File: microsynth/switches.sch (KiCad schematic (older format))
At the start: 39 parts, among them SW12 SW_DP3T, SW13 SW_DP3T, SW14 SW_SPDT, SW15 SW_SPDT, SW16 SW_SPDT, SW17 SW_SPDT, SW2 SW_Rotary2x6, SW21 SW_Rotary2x6, SW3 SW_DP3T, SW4 SW_DP3T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

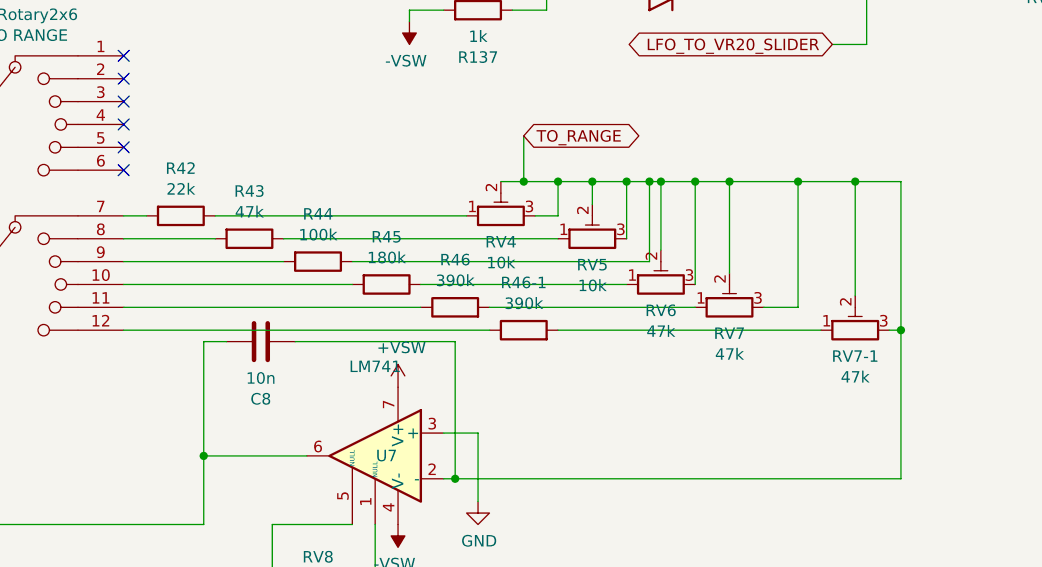
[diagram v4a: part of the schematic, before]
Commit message: Replace IC1 with LM348, update component values
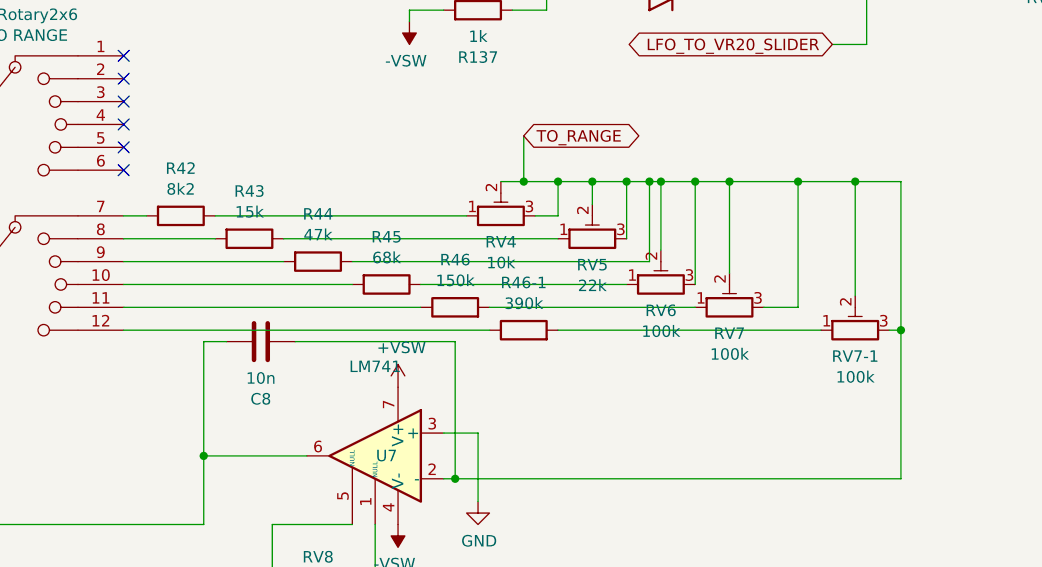
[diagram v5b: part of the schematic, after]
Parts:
- R42: value 22k -> 8k2
- R43: value 47k -> 15k
- R44: value 100k -> 47k
- R45: value 180k -> 68k
- R46: value 390k -> 150k
- RV5: value 10k -> 22k
- RV6, RV7, RV7-1: value 47k -> 100k
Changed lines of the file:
@@
 P 2450 5750
 F 0 "R42" V 2243 5750 50  0000 C CNN
-F 1 "22k" V 2334 5750 50  0000 C CNN
+F 1 "8k2" V 2334 5750 50  0000 C CNN
 F 2 "Resistor_THT:R_Axial_DIN0207_L6.3mm_D2.5mm_P10.16mm_Horizontal" V 2380 5750 50  0001 C CNN
 F 3 "~" H 2450 5750 50  0001 C CNN
@@
 P 2750 5850
 F 0 "R43" V 2543 5850 50  0000 C CNN
-F 1 "47k" V 2634 5850 50  0000 C CNN
+F 1 "15k" V 2634 5850 50  0000 C CNN
 F 2 "Resistor_THT:R_Axial_DIN0207_L6.3mm_D2.5mm_P10.16mm_Horizontal" V 2680 5850 50  0001 C CNN
 F 3 "~" H 2750 5850 50  0001 C CNN
@@
 P 3050 5950
 F 0 "R44" V 2843 5950 50  0000 C CNN
-F 1 "100k" V 2934 5950 50  0000 C CNN
+F 1 "47k" V 2934 5950 50  0000 C CNN
 F 2 "Resistor_THT:R_Axial_DIN0207_L6.3mm_D2.5mm_P10.16mm_Horizontal" V 2980 5950 50  0001 C CNN
 F 3 "~" H 3050 5950 50  0001 C CNN
@@
 P 3350 6050
 F 0 "R45" V 3143 6050 50  0000 C CNN
-F 1 "180k" V 3234 6050 50  0000 C CNN
+F 1 "68k" V 3234 6050 50  0000 C CNN
 F 2 "Resistor_THT:R_Axial_DIN0207_L6.3mm_D2.5mm_P10.16mm_Horizontal" V 3280 6050 50  0001 C CNN
 F 3 "~" H 3350 6050 50  0001 C CNN
@@
 P 3650 6150
 F 0 "R46" V 3857 6150 50  0000 C CNN
-F 1 "390k" V 3766 6150 50  0000 C CNN
+F 1 "150k" V 3766 6150 50  0000 C CNN
 F 2 "Resistor_THT:R_Axial_DIN0207_L6.3mm_D2.5mm_P10.16mm_Horizontal" V 3580 6150 50  0001 C CNN
 F 3 "~" H 3650 6150 50  0001 C CNN
@@
 P 4250 5850
 F 0 "RV5" V 4135 5850 50  0000 C CNN
-F 1 "10k" V 4044 5850 50  0000 C CNN
+F 1 "22k" V 4044 5850 50  0000 C CNN
 F 2 "Potentiometers:Potentiometer_Trimmer_Bourns_PV36W" H 4250 5850 50  0001 C CNN
 F 3 "~" H 4250 5850 50  0001 C CNN
@@
 P 4550 6050
 F 0 "RV6" V 4435 6050 50  0000 C CNN
-F 1 "47k" V 4344 6050 50  0000 C CNN
+F 1 "100k" V 4344 6050 50  0000 C CNN
 F 2 "Potentiometers:Potentiometer_Trimmer_Bourns_PV36W" H 4550 6050 50  0001 C CNN
 F 3 "~" H 4550 6050 50  0001 C CNN
@@
 P 4850 6150
 F 0 "RV7" V 4735 6150 50  0000 C CNN
-F 1 "47k" V 4644 6150 50  0000 C CNN
+F 1 "100k" V 4644 6150 50  0000 C CNN
 F 2 "Potentiometers:Potentiometer_Trimmer_Bourns_PV36W" H 4850 6150 50  0001 C CNN
 F 3 "~" H 4850 6150 50  0001 C CNN
@@
 P 5400 6250
 F 0 "RV7-1" V 5285 6250 50  0000 C CNN
-F 1 "47k" V 5194 6250 50  0000 C CNN
+F 1 "100k" V 5194 6250 50  0000 C CNN
 F 2 "Potentiometers:Potentiometer_Trimmer_Bourns_PV36W" H 5400 6250 50  0001 C CNN
 F 3 "~" H 5400 6250 50  0001 C CNN

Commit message: Annotate schematic
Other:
- note added: "KBD"
- note added: "OFF ONE TWO"
- note added: "SUBOCTAVES"
- note added: "TRI SAW SQR"
- note added: "VCA"
- note added: "VCF"
- note added: "VCO RM LFO"
- note added: "VCO1 SHAPE"
- note added: "VCO1 SQR"
- note added: "VCO1 VCO2"
- note added: "VCO2 SHAPE"
- note added: "VCO2/LFO MOD"
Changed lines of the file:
@@
 	7550 2150 7550 1550
 Wire Wire Line
-	8700 800  8550 800
-Wire Wire Line
-	8550 800  8550 1750
+	8700 550  8550 550
+Wire Wire Line
+	8550 550  8550 1750
 Connection ~ 8550 1750
 Wire Wire Line
@@
 Text GLabel 7250 600  2    50   BiDi ~ 0
 TO_VCA_C26
-Text GLabel 8700 800  2    50   BiDi ~ 0
+Text GLabel 8700 550  2    50   BiDi ~ 0
 TO_VCF_IC20_3
 Text GLabel 6950 800  0    50   BiDi ~ 0
@@
 F 2 "microsynth:11-SS-23-832C" H 9150 1250 50  0001 C CNN
 F 3 "" H 9150 1250 50  0001 C CNN
-F 4 "SUBOCTAVES" H 9250 1600 50  0000 C CNN "Label"
+F 4 "SUBOCTAVES" H 9150 1800 50  0000 C CNN "Label"
 	2    9150 1250
 	1    0    0    -1
@@
 Wire Wire Line
 	2800 1700 3250 1700
+Text Notes 1200 1250 0    50   ~ 0
+VCO2 SHAPE
+Text Notes 2950 550  0    50   ~ 0
+VCO2/LFO MOD
+Text Notes 3850 900  0    50   ~ 0
+KBD
+Text Notes 3850 1400 0    50   ~ 0
+VCO1 SQR
+Text Notes 3850 1900 0    50   ~ 0
+VCF
+Text Notes 3850 2400 0    50   ~ 0
+VCA
+Text Notes 2450 3200 0    50   ~ 0
+VCO RM LFO
+Text Notes 5850 3150 0    50   ~ 0
+VCO RM LFO
+Text Notes 7150 950  0    50   ~ 0
+TRI SAW SQR
+Text Notes 7150 750  0    50   ~ 0
+VCO1 SHAPE
+Text Notes 8900 900  0    50   ~ 0
+OFF ONE TWO
+Text Notes 10450 700  0    50   ~ 0
+SUBOCTAVES
+Text Notes 10450 900  0    50   ~ 0
+VCO1 VCO2
 $EndSCHEMATC
